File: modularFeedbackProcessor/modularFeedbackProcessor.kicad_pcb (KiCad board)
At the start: 2 copper layers, 209 parts, among them J1 Input, J10 Output, J2 Feedback, J3 Inhibit, J4 Eurorack_Power_16pin_Unshroud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, J5 DryWet, J6 Rate, J7 EffectsRouteIn, J8 EffectsRouteOut, J9 EffectsDryWet, Q1 Q_PMOS_GDS, Q10 Q_PMOS_GDS, Q11 Q_NMOS_GDS, Q12 Q_PMOS_GDS, Q13 Q_PMOS_GDS, Q14 Q_NMOS_GDS, Q15 Q_PMOS_GDS, Q16 Q_NMOS_GDS, Q17 Q_PMOS_GDS, Q18 Q_NMOS_GDS, Q19 Q_PMOS_GDS, Q2 Q_NMOS_GDS, Q3 Q_PMOS_GDS, Q4 Q_PMOS_GDS, Q5 Q_NMOS_GDS, Q6 Q_PMOS_GDS, Q7 Q_NMOS_GDS, Q8 Q_PMOS_GDS, Q9 Q_NMOS_GDS, SW1 EffectsRouting, U1 TL074, U10 LM13700, U2 TL074, U3 TL074, U4 LM13700, U5 V3205, U6 CD4046, U7 LF398_DIP8, U8 LM13700, U9 TL074

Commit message: save before i mess something up
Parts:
- TP5: value BBDOut -> S&HOut
- moved D8 224.3 mm to (390.1, -0.36)
- moved R41 224.3 mm to (390.9, -23.6)
- moved R44 224.3 mm to (390.9, -14.7)
- moved R46 224.3 mm to (395.7, -23.6)
- moved R49 224.3 mm to (395.7, -14.7)
- moved R51 224.3 mm to (400.4, -23.6)
- moved R54 224.3 mm to (400.4, -14.7)
- moved R56 224.3 mm to (405.2, -23.6)
- moved R59 224.3 mm to (405.2, -14.7)
- moved RV12 224.3 mm to (391.7, -8.75)
- moved RV13 224.3 mm to (397.9, -8.75)
- moved RV14 224.3 mm to (404.2, -8.75)
- moved R42 224.3 mm to (390.9, -20.6)
- moved R43 224.3 mm to (390.9, -17.7)
- moved R45 224.3 mm to (390.9, -11.8)
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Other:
- copper layers 2 -> 4

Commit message: layout mostly down. Going to begin routing
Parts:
- removed the C10 at (387.5, -38.6)
- removed the C11 at (323.5, -30.5)
- removed the C12 at (282.5, -40.0)
- removed the C13 at (291.1, -19.7)
- removed the C14 at (300.1, -35.2)
- removed the C15 at (302.6, -19.7)
- removed C35, C36: 100n, Capacitor_SMD:C_0805_2012Metric_Pad1.18x1.45mm_HandSolder
- removed the C6 at (387.5, -50.6)
- removed the C7 at (387.5, -47.6)
- removed the C8 at (387.5, -44.6)
- removed the C9 at (387.5, -41.6)
- removed the D2 at (41.8, 147.5)
- removed the D3 at (29.5, 158.1)
- removed the D8 at (390.1, -0.36)
- removed the D9 at (312.2, -25.0)
- removed J3: Inhibit, PCM_Eurocad:PJ301M-12
- removed the R41 at (390.9, -23.6)
- removed the R42 at (390.9, -20.6)
- removed the R43 at (390.9, -17.7)
- removed the R9 at (30.0, 162.0)
- removed the TP6 at (322.8, 65.2)
- removed the U1 at (403.4, -50.1)
- added C17: 1n, Capacitor_SMD:C_0805_2012Metric_Pad1.18x1.45mm_HandSolder, F.Cu at (157.7, 67.6)
- added C18: 2.2u, Capacitor_SMD:C_0805_2012Metric_Pad1.18x1.45mm_HandSolder, F.Cu at (116.7, 58.1)
- added C19: 2.2u, Capacitor_SMD:C_0805_2012Metric_Pad1.18x1.45mm_HandSolder, F.Cu at (125.4, 78.4)
- added C22: 100n, Capacitor_SMD:C_0805_2012Metric_Pad1.18x1.45mm_HandSolder, F.Cu at (143.7, 62.1)
- added C23: 100n, Capacitor_SMD:C_0805_2012Metric_Pad1.18x1.45mm_HandSolder, F.Cu at (157.7, 62.1)
- added C24: 100n, Capacitor_SMD:C_0805_2012Metric_Pad1.18x1.45mm_HandSolder, F.Cu at (129.4, 62.9)
- added C25: 100n, Capacitor_SMD:C_0805_2012Metric_Pad1.18x1.45mm_HandSolder, F.Cu at (129.4, 78.4)
- added C26: 1n, Capacitor_SMD:C_0805_2012Metric_Pad1.18x1.45mm_HandSolder, F.Cu at (214.5, 134.4)
- added C27: 2.2u, Capacitor_SMD:C_0805_2012Metric_Pad1.18x1.45mm_HandSolder, F.Cu at (224.0, 93.4)
- added C28: 2.2u, Capacitor_SMD:C_0805_2012Metric_Pad1.18x1.45mm_HandSolder, F.Cu at (203.8, 102.1)
- added C29: 2.2u, Capacitor_SMD:C_0805_2012Metric_Pad1.18x1.45mm_HandSolder, F.Cu at (219.2, 111.1)
- added C30: 2.2u, Capacitor_SMD:C_0805_2012Metric_Pad1.18x1.45mm_HandSolder, F.Cu at (203.7, 113.6)
- added D11: 1N4148, Diode_THT:D_DO-35_SOD27_P7.62mm_Horizontal, F.Cu at (146.4, 73.1)
- added D12: 1N4148, Diode_THT:D_DO-35_SOD27_P7.62mm_Horizontal, F.Cu at (209.0, 123.1)
- added R81: 1k, Resistor_SMD:R_0805_2012Metric_Pad1.20x1.40mm_HandSolder, F.Cu at (222.7, 110.1)
- added R82: 1k, Resistor_SMD:R_0805_2012Metric_Pad1.20x1.40mm_HandSolder, F.Cu at (203.7, 111.1)
- added R83: 1k, Resistor_SMD:R_0805_2012Metric_Pad1.20x1.40mm_HandSolder, F.Cu at (226.2, 110.1)
- added U7: TL074, Package_DIP:DIP-14_W7.62mm_LongPads, F.Cu at (146.7, 53.5)
- C20, C21: value 100n -> 2.2u
- R44, R45, R64, R65: value 560 -> 18k
- R46, R66: value 12k -> 18k
- R47, R67: value 12k -> 560
- R48, R68: value 33k -> 560
- R49, R50, R69, R70: value 560 -> 12k
- R51, R71: value 1k -> 33k
- R52, R53, R72, R73: value 5.6k -> 560
- R54, R74: value 100k -> 1k
- R55, R75: value 100k -> 5.6k
- R56, R76: value 6.8k -> 5.6k
- R57, R77: value 6.8k -> 100k
- R58, R78: value 1k -> 100k
- R59, R60, R79, R80: value 1k -> 6.8k
- R61, R62, R63: value 18k -> 1k
- TP12: value MixTune1 -> MixerV1
- TP13: value MixTune1 -> MixerV2
- TP14: value MixerV1 -> MixTune1
- TP15: value MixerV1 -> MixerV1o
- TP16: value MixerV2 -> MixerV2o
- TP17: value MixerV2 -> MixerOut
- TP18: value MixerV1o -> MixerV1
- TP19: value MixerV1o -> MixerV2
- TP20: value MixerV2o -> MixTune1
- TP21: value MixerV2o -> MixerV1o
- TP22: value MixerOut -> MixerV2o
- moved R60 304.6 mm to (112.9, 73.9)
- moved U8 301.9 mm to (116.8, 74.4), turned to 90 degrees
- moved R48 295.2 mm to (117.4, 80.9), turned to 180 degrees
- moved R53 293.3 mm to (124.9, 82.9)
- moved R50 292.2 mm to (117.4, 77.4), turned to 180 degrees
- moved R46 292.2 mm to (121.9, 78.4), turned to 90 degrees
- moved R47 289.6 mm to (118.4, 62.9), turned to 90 degrees
- moved RV14 289.0 mm to (129.9, 82.3)
- moved R58 287.4 mm to (135.9, 82.9), turned to 180 degrees
- moved TP12 286.8 mm to (113.2, 62.6)
- moved R52 283.6 mm to (127.9, 57.9), turned to 90 degrees
- moved R56 282.9 mm to (138.9, 71.9), turned to 90 degrees
- moved R49 281.2 mm to (125.4, 62.9), turned to -90 degrees
- moved Q8 280.9 mm to (116.7, 93.5)
- moved RV13 280.4 mm to (125.2, 56.6), turned to -90 degrees
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- renumbered C18 to C1, C3 to C10, C29 to C11, C30 to C12, C28 to C13, C4 to C14, C26 to C15, C5 to C16, C19 to C2, C24 to C3, C25 to C4, C22 to C5, C23 to C6, C1 to C7, C2 to C8, C27 to C9, D10 to D1, D7 to D10, D12 to D2, D11 to D3, D1 to D4, D4 to D7, D5 to D8, D6 to D9, R81 to R1, R7 to R10, R8 to R11, R10 to R13, R11 to R14, R12 to R15, R13 to R16, R14 to R17, R15 to R18, R16 to R19, R82 to R2, R17 to R20, R18 to R21, R19 to R22, R20 to R23, R21 to R24, R22 to R25, R23 to R26, R24 to R27, R25 to R28, R26 to R29, R1 to R3, R27 to R30, R28 to R31, R29 to R32, R30 to R33, R31 to R34, R32 to R35, R33 to R36, R34 to R37, R35 to R38, R36 to R39, R83 to R4, R37 to R40, R38 to R41, R39 to R42, R40 to R43, R2 to R5, R3 to R6, R4 to R7, R5 to R8, R6 to R9, TP10 to TP1, TP4 to TP10, TP3 to TP2, TP11 to TP3, TP1 to TP4, TP2 to TP5, TP8 to TP6, TP9 to TP7, TP5 to TP8, TP7 to TP9, U2 to U1, U3 to U2, U4 to U3, U5 to U4, U6 to U5, U7 to U6
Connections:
- C20 pad 1: +12V -> Net-(C20-Pad1)
- C20 pad 2: GND -> Net-(C20-Pad2)
- C21 pad 1: GND -> Net-(C21-Pad1)
- C21 pad 2: -12V -> Net-(C21-Pad2)
- C31 pad 1: GND -> +12V
- C31 pad 2: -12V -> GND
- C34 pad 1: +12V -> GND
- C34 pad 2: GND -> -12V
- J7 pad 1: /Effects Mixer/V_{in2} -> /Mixer2/V_{in2}
- R36 pad 2: /DryWet Mixer/V_{ctrl} -> /Mixer1/V_{ctrl}
- R37 pad 2: /DryWet Mixer/V_{ctrl} -> /Mixer1/V_{ctrl}
- R38 pad 1: /DryWet Mixer/V_{in2} -> /Mixer1/V_{in2}
- R39 pad 2: /Effects Mixer/V_{ctrl} -> /Mixer2/V_{ctrl}
- R40 pad 2: /Effects Mixer/V_{ctrl} -> /Mixer2/V_{ctrl}
- R41 pad 1: /DryWet Mixer/V_{out} -> /Mixer1/V_{out}
- R44 pad 1: Net-(U8A-+) -> -12V
- R44 pad 2: GND -> Net-(R44-Pad2)
- R45 pad 1: Net-(U8C-+) -> Net-(C18-Pad2)
- R45 pad 2: GND -> Net-(U8A-+)
- R46 pad 1: Net-(U8A-DIODE_BIAS) -> Net-(C19-Pad2)
- R46 pad 2: +12V -> Net-(U8C-+)
- R47 pad 1: Net-(U8C-DIODE_BIAS) -> Net-(U8A-+)
- R47 pad 2: +12V -> GND
- R48 pad 1: /DryWet Mixer/V_{ctrl} -> Net-(U8C-+)
- R48 pad 2: Net-(Q3-S) -> GND
- R49 pad 1: Net-(U8A--) -> Net-(U8A-DIODE_BIAS)
- R49 pad 2: GND -> +12V
- R50 pad 1: Net-(U8C--) -> Net-(U8C-DIODE_BIAS)
- R50 pad 2: GND -> +12V
- R51 pad 1: Net-(Q3-S) -> /Mixer1/V_{ctrl}
- R51 pad 2: GND -> Net-(Q3-S)
- R52 pad 1: Net-(C9-Pad1) -> Net-(U8A--)
- R52 pad 2: -12V -> GND
- R53 pad 1: Net-(C10-Pad1) -> Net-(U8C--)
- R53 pad 2: -12V -> GND
- R54 pad 1: Net-(C9-Pad2) -> Net-(Q3-S)
- R55 pad 1: Net-(C10-Pad2) -> Net-(C20-Pad1)
- R55 pad 2: GND -> -12V
- R56 pad 1: Net-(Q6-D) -> Net-(C21-Pad1)
- R56 pad 2: /DryWet Mixer/Iout2 -> -12V
- R57 pad 1: Net-(Q10-D) -> Net-(C20-Pad2)
- R57 pad 2: /DryWet Mixer/Iout1 -> GND
- R58 pad 1: Net-(C9-Pad2) -> Net-(C21-Pad2)
- R58 pad 2: Net-(U1A--) (its old number) -> GND
- R59 pad 1: Net-(C10-Pad2) -> Net-(Q6-D)
- R59 pad 2: Net-(U1A--) (its old number) -> /Mixer1/Iout2
- R60 pad 1: Net-(U1A--) (its old number) -> Net-(Q10-D)
- R60 pad 2: /DryWet Mixer/V_{out} -> /Mixer1/Iout1
- R61 pad 1: -12V -> Net-(C20-Pad2)
- R61 pad 2: Net-(R61-Pad2) -> Net-(U7A--)
- R62 pad 1: Net-(C12-Pad2) -> Net-(C21-Pad2)
- R62 pad 2: Net-(U10A-+) -> Net-(U7A--)
- R63 pad 1: Net-(C13-Pad2) -> Net-(U7A--)
- R63 pad 2: Net-(U10C-+) -> /Mixer1/V_{out}
- R64 pad 1: Net-(U10A-+) -> -12V
- R64 pad 2: GND -> Net-(R64-Pad2)
- R65 pad 1: Net-(U10C-+) -> Net-(C27-Pad2)
- R65 pad 2: GND -> Net-(U10A-+)
- R66 pad 1: Net-(U10A-DIODE_BIAS) -> Net-(C28-Pad2)
- R66 pad 2: +12V -> Net-(U10C-+)
- R67 pad 1: Net-(U10C-DIODE_BIAS) -> Net-(U10A-+)
- R67 pad 2: +12V -> GND
- R68 pad 1: /Effects Mixer/V_{ctrl} -> Net-(U10C-+)
- R68 pad 2: Net-(Q12-S) -> GND
- R69 pad 1: Net-(U10A--) -> Net-(U10A-DIODE_BIAS)
- R69 pad 2: GND -> +12V
- R70 pad 1: Net-(U10C--) -> Net-(U10C-DIODE_BIAS)
- R70 pad 2: GND -> +12V
- R71 pad 1: Net-(Q12-S) -> /Mixer2/V_{ctrl}
- R71 pad 2: GND -> Net-(Q12-S)
- R72 pad 1: Net-(C14-Pad1) -> Net-(U10A--)
- R72 pad 2: -12V -> GND
- R73 pad 1: Net-(C15-Pad1) -> Net-(U10C--)
- R73 pad 2: -12V -> GND
- R74 pad 1: Net-(C14-Pad2) -> Net-(Q12-S)
- R75 pad 1: Net-(C15-Pad2) -> Net-(C29-Pad1)
- R75 pad 2: GND -> -12V
- R76 pad 1: Net-(Q15-D) -> Net-(C30-Pad1)
- R76 pad 2: /Effects Mixer/Iout2 -> -12V
- R77 pad 1: Net-(Q19-D) -> Net-(C29-Pad2)
- R77 pad 2: /Effects Mixer/Iout1 -> GND
- R78 pad 1: Net-(C14-Pad2) -> Net-(C30-Pad2)
- R78 pad 2: Net-(U9A--) -> GND
- R79 pad 1: Net-(C15-Pad2) -> Net-(Q15-D)
- R79 pad 2: Net-(U9A--) -> /Mixer2/Iout2
- R80 pad 1: Net-(U9A--) -> Net-(Q19-D)
- R80 pad 2: /Effects Mixer/V_{out} -> /Mixer2/Iout1
- RV12 pad 1: Net-(R41-Pad2) -> Net-(R44-Pad2)
- RV12 pad 2: Net-(R41-Pad2) -> Net-(R44-Pad2)
- RV15 pad 1: Net-(R61-Pad2) -> Net-(R64-Pad2)
- RV15 pad 2: Net-(R61-Pad2) -> Net-(R64-Pad2)
- RV2 pad 1: /DryWet Mixer/V_{in1} -> /Mixer1/V_{in1}
- SW1 pad 1: /DryWet Mixer/V_{in2} -> /Mixer1/V_{in2}
- SW1 pad 3: /Effects Mixer/V_{out} -> /Mixer2/V_{out}
- TP10 pad 1: /DryWet Mixer/V_{in1} -> /Mixer1/V_{in1}
- TP12 pad 1: Net-(Q2-S) -> /Mixer1/V_{in1}
- TP13 pad 1: Net-(Q11-S) -> /Mixer1/V_{in2}
- TP14 pad 1: /DryWet Mixer/V_{in1} -> Net-(Q2-S)
- TP15 pad 1: /DryWet Mixer/V_{in2} -> Net-(C20-Pad2)
- TP16 pad 1: /DryWet Mixer/V_{in2} -> Net-(C21-Pad2)
- TP17 pad 1: /Effects Mixer/V_{in2} -> /Mixer1/V_{out}
- TP18 pad 1: Net-(C9-Pad2) -> /Mixer1/V_{in2}
- TP19 pad 1: Net-(C14-Pad2) -> /Mixer2/V_{in2}
- TP20 pad 1: Net-(C10-Pad2) -> Net-(Q11-S)
- TP21 pad 1: Net-(C15-Pad2) -> Net-(C29-Pad2)
- TP22 pad 1: /DryWet Mixer/V_{out} -> Net-(C30-Pad2)
- TP23 pad 1: /Effects Mixer/V_{out} -> /Mixer2/V_{out}
- TP9 pad 1: /Effects Mixer/V_{out} -> /Mixer2/V_{out}
- U1 pad 13: /DryWet Mixer/V_{in1} -> /Mixer1/V_{in1}
- U1 pad 14: /DryWet Mixer/V_{in1} -> /Mixer1/V_{in1}
- U10 pad 1: /Effects Mixer/Iout1 -> /Mixer2/Iout1
- U10 pad 16: /Effects Mixer/Iout2 -> /Mixer2/Iout2
- U10 pad 8: Net-(C15-Pad1) -> Net-(C30-Pad1)
- U10 pad 9: Net-(C14-Pad1) -> Net-(C29-Pad1)
- U2 pad 13: /DryWet Mixer/V_{in2} -> /Mixer1/V_{in2}
- U2 pad 14: /DryWet Mixer/V_{in2} -> /Mixer1/V_{in2}
- U5 pad 5: Net-(D2-A) (its old number) -> GND
- U8 pad 1: /DryWet Mixer/Iout1 -> /Mixer1/Iout1
- U8 pad 16: /DryWet Mixer/Iout2 -> /Mixer1/Iout2
- U8 pad 8: Net-(C10-Pad1) -> Net-(C21-Pad1)
- U8 pad 9: Net-(C9-Pad1) -> Net-(C20-Pad1)
- U9 pad 1: /Effects Mixer/V_{out} -> /Mixer2/V_{out}
- U9 pad 9: /Effects Mixer/V_{ctrl} -> /Mixer2/V_{ctrl}

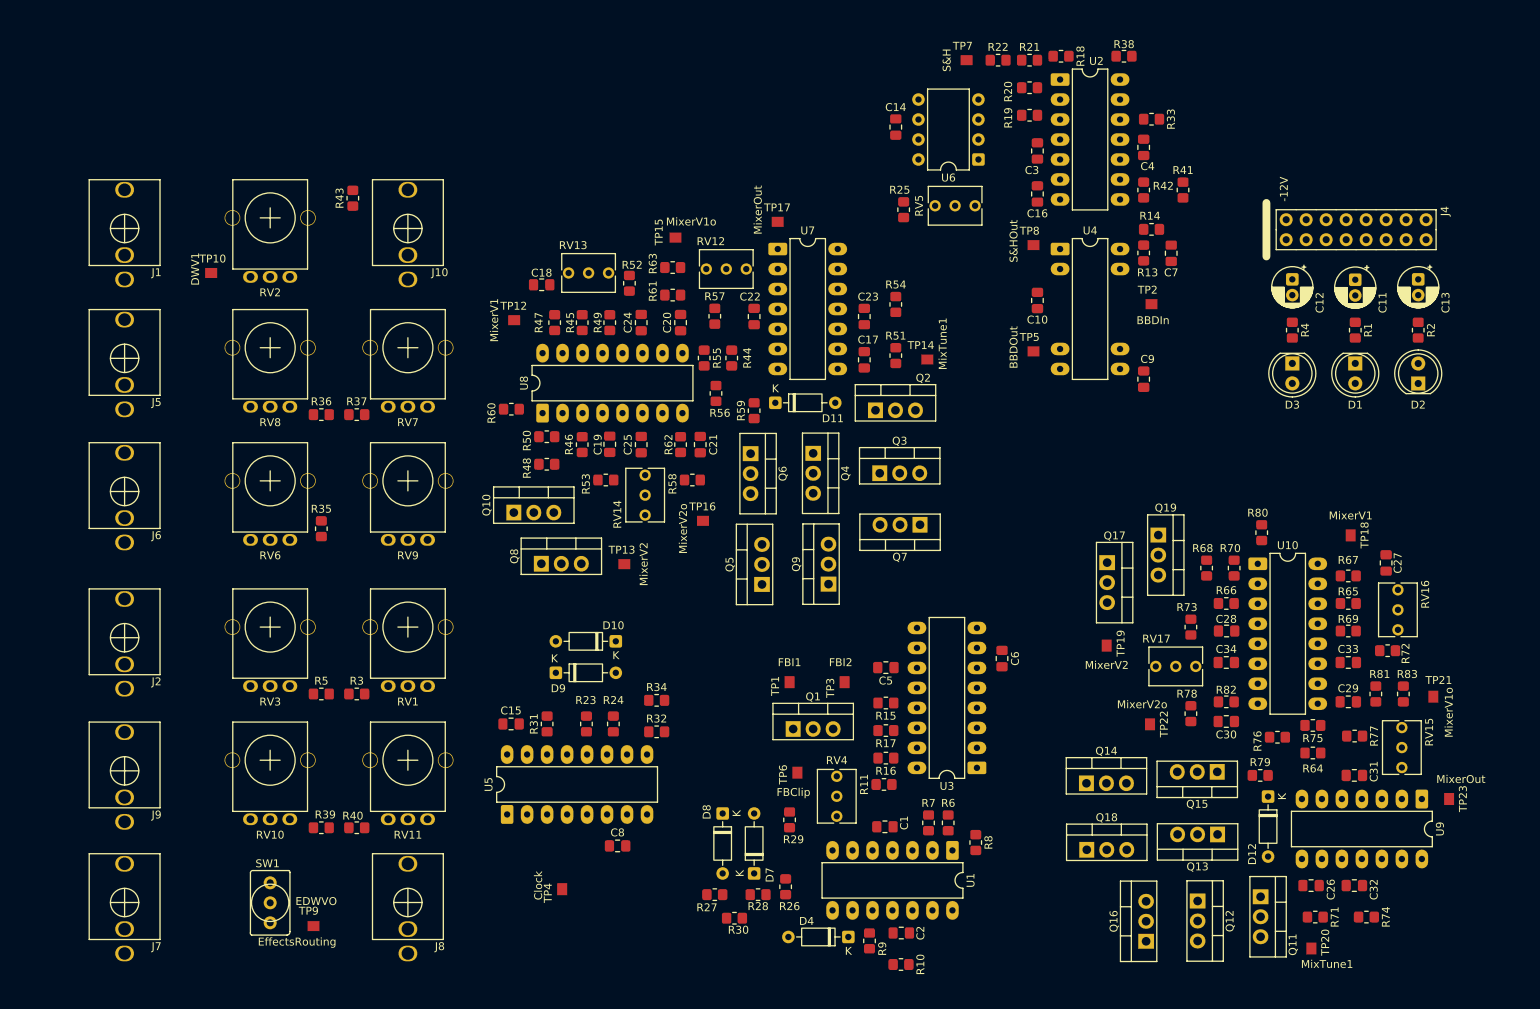
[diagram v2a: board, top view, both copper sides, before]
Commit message: routed power, good start
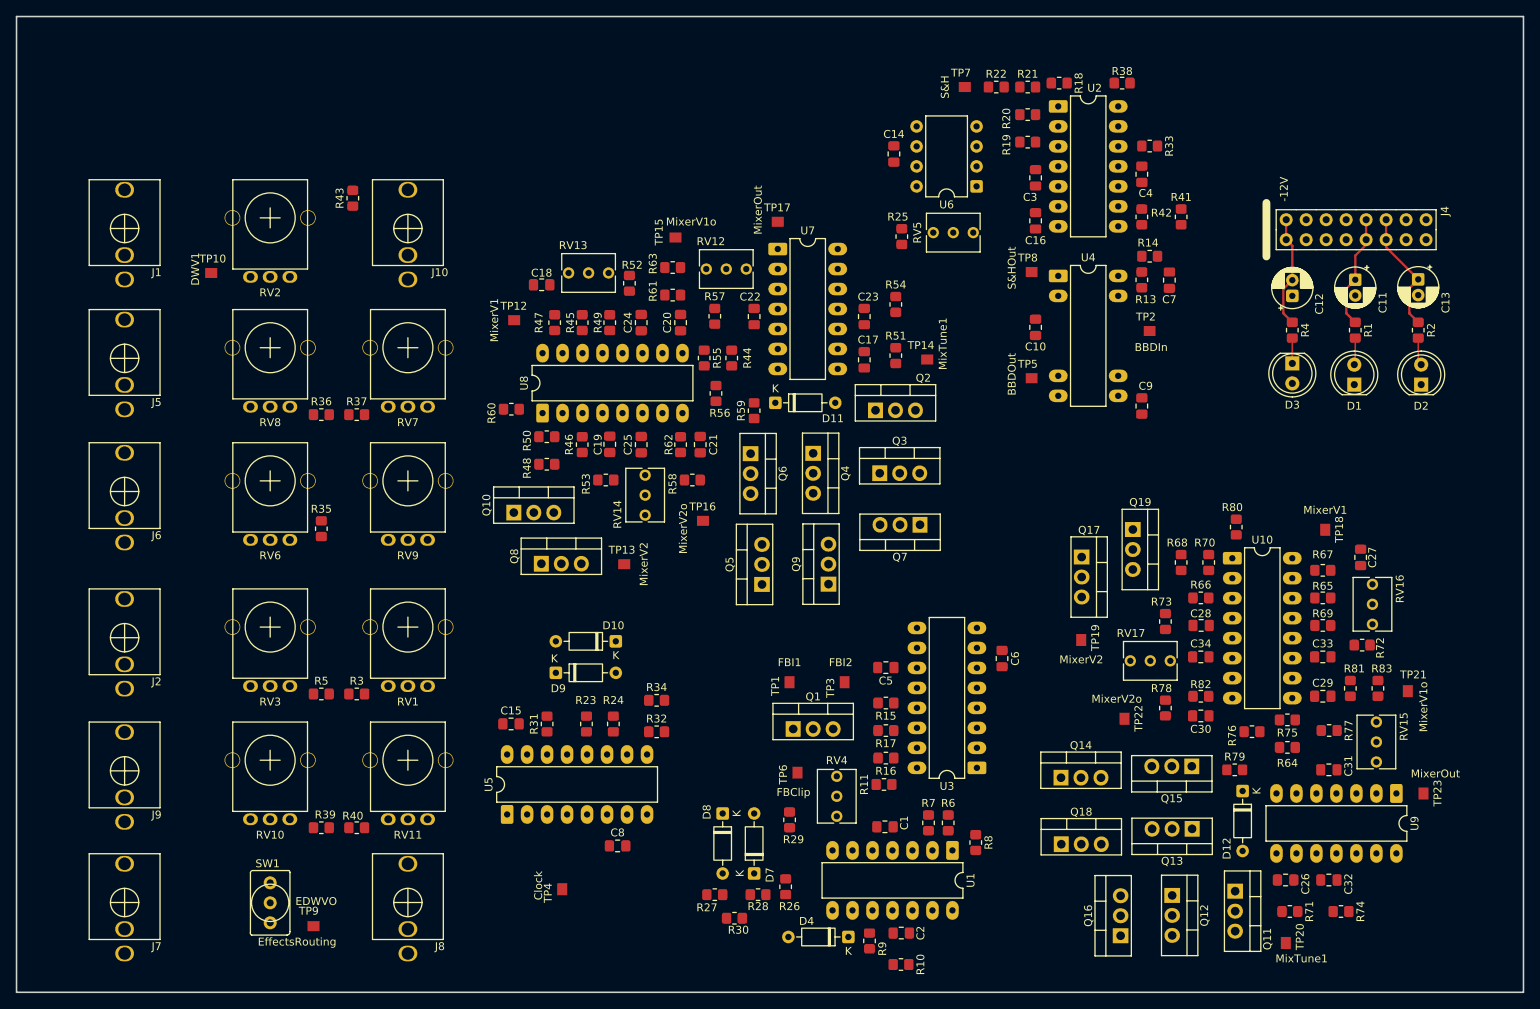
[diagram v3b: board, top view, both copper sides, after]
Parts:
- moved D2 8.80 mm to (228.5, 70.8), turned to 90 degrees
- moved D1 8.13 mm to (220.0, 70.8)
- moved C10 3.42 mm to (179.5, 63.5)
- moved C3 3.42 mm to (179.5, 44.5)
- moved C7 3.42 mm to (196.5, 57.5)
- moved C9 3.42 mm to (193.0, 73.5)
- moved TP5 3.42 mm to (179.0, 70.0)
- moved U2 3.42 mm to (182.4, 35.4)
- moved U6 3.42 mm to (172.0, 45.6)
- moved R18 3.42 mm to (182.5, 32.5)
- moved R21 3.42 mm to (178.5, 33.0)
- moved R22 3.42 mm to (174.5, 33.0)
- moved R38 3.42 mm to (190.5, 32.5)
- moved TP7 3.42 mm to (170.5, 33.0)
- moved C14 3.42 mm to (161.5, 41.5)
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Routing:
- net +5V: track 0.00 -> 15.7 mm
- net +12V: track 0.00 -> 14.5 mm
- net -12V: track 0.00 -> 14.3 mm
- net Net-(D2-A): track 0.00 -> 3.53 mm
- net Net-(D1-A): track 0.00 -> 3.43 mm
- net Net-(D3-K): track 0.00 -> 3.22 mm
- added copper zone on In2.Cu, net GND
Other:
- board outline added: 191.5 x 124 mm

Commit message: mostly done with the BBD module routing
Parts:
- moved C14 50.4 mm to (205.1, 66.9)
- moved TP7 43.9 mm to (200.0, 65.5), turned to 180 degrees
- moved R25 40.7 mm to (203.1, 48.9)
- moved C9 40.6 mm to (191.6, 32.9), turned to 0 degrees
- moved R22 39.0 mm to (196.0, 65.5), turned to 180 degrees
- moved R21 35.2 mm to (192.0, 65.5), turned to 180 degrees
- moved R38 35.1 mm to (180.0, 66.0), turned to 180 degrees
- moved TP2 34.0 mm to (182.6, 31.9), turned to 90 degrees
- moved R18 34.0 mm to (188.0, 66.0), turned to 0 degrees
- moved RV5 33.8 mm to (200.1, 47.9), turned to -90 degrees
- moved TP5 32.9 mm to (195.5, 41.5), turned to -90 degrees
- moved R14 30.4 mm to (172.6, 32.9), turned to -90 degrees
- moved C7 30.3 mm to (172.6, 38.9), turned to 90 degrees
- moved R13 29.7 mm to (177.1, 32.4), turned to 180 degrees
- moved R20 28.9 mm to (192.0, 62.0), turned to 0 degrees
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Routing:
- net Net-(U4-OUT1): track 0.00 -> 27.5 mm, vias 0 -> 2
- net Net-(U4-CP1): track 0.00 -> 21.4 mm
- net Net-(U6-T): track 0.00 -> 20.8 mm
- net Net-(U2B-+): track 0.00 -> 20.0 mm, vias 0 -> 1
- net Net-(U2D-+): track 0.00 -> 17.2 mm
- net +12V: track 14.5 -> 31.5 mm
- net +5V: track 15.7 -> 32.4 mm
- net Net-(R21-Pad2): track 0.00 -> 13.7 mm
- net GND: track 0.00 -> 13.5 mm, vias 0 -> 6
- net Net-(U2B--): track 0.00 -> 13.1 mm
- net Net-(U4-V_{GG}): track 0.00 -> 12.7 mm
- net Net-(U2A-+): track 0.00 -> 11.1 mm, vias 0 -> 1
- net Net-(U2A--): track 0.00 -> 10.6 mm
- net Net-(U6-Adj): track 0.00 -> 8.50 mm
- net Net-(U6-C_{h}): track 0.00 -> 8.45 mm
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- added copper zone on B.Cu, net GND
- removed copper zone on In2.Cu, net GND
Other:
- copper layers 4 -> 2

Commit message: significant progress
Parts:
- removed TP10: DWV1, PCM_4ms_TestPoint:TestPoint_Pad_06
- moved J4 81.2 mm to (233.5, 125.7), turned to 0 degrees
- moved C12 80.5 mm to (225.3, 133.4), turned to 0 degrees
- moved TP4 77.0 mm to (179.0, 81.0)
- moved R4 75.5 mm to (220.3, 133.4), turned to 180 degrees
- moved C8 74.0 mm to (186.1, 80.5)
- moved C11 73.9 mm to (227.2, 125.5), turned to 180 degrees
- moved C15 73.3 mm to (172.6, 66.3)
- moved D9 73.3 mm to (178.3, 59.8)
- moved R24 73.3 mm to (185.6, 66.3)
- moved U5 73.3 mm to (172.1, 77.8)
- moved R23 73.3 mm to (182.2, 66.3)
- moved R31 73.3 mm to (177.2, 66.3)
- moved R32 73.3 mm to (191.1, 67.3)
- moved R34 73.3 mm to (191.1, 63.3)
- moved D10 73.3 mm to (185.9, 55.8)
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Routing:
- net -12V: track 17.4 -> 417.3 mm, vias 0 -> 6
- net +12V: track 31.5 -> 410.3 mm, vias 0 -> 10
- net +5V: track 32.4 -> 276.0 mm, vias 0 -> 2
- net /Mixer2/V_{out}: track 0.00 -> 160.2 mm, vias 0 -> 2
- net Net-(J8-T): track 0.00 -> 142.0 mm, vias 0 -> 9
- net Net-(R32-Pad2): track 0.00 -> 120.4 mm, vias 0 -> 12
- net /Mixer1/V_{in1}: track 0.00 -> 105.6 mm, vias 0 -> 7
- net Net-(U4-IN): track 6.11 -> 97.9 mm, vias 0 -> 6
- net /Mixer1/V_{out}: track 0.00 -> 85.6 mm, vias 0 -> 2
- net Net-(SW1-B): track 0.00 -> 58.4 mm
- net Net-(Q10-G): track 0.00 -> 57.5 mm, vias 0 -> 3
- net Net-(Q16-D): track 0.00 -> 56.7 mm, vias 0 -> 3
- net GND: track 13.5 -> 67.4 mm, vias 6 -> 20
- net Net-(U4-CP1): track 21.4 -> 67.7 mm
- net Net-(Q2-S): track 0.00 -> 39.3 mm
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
